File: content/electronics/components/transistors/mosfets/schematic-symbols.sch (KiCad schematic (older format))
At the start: 3 parts, among them Q1 Q_NMOS_DGS, Q2 Q_PMOS_DGS

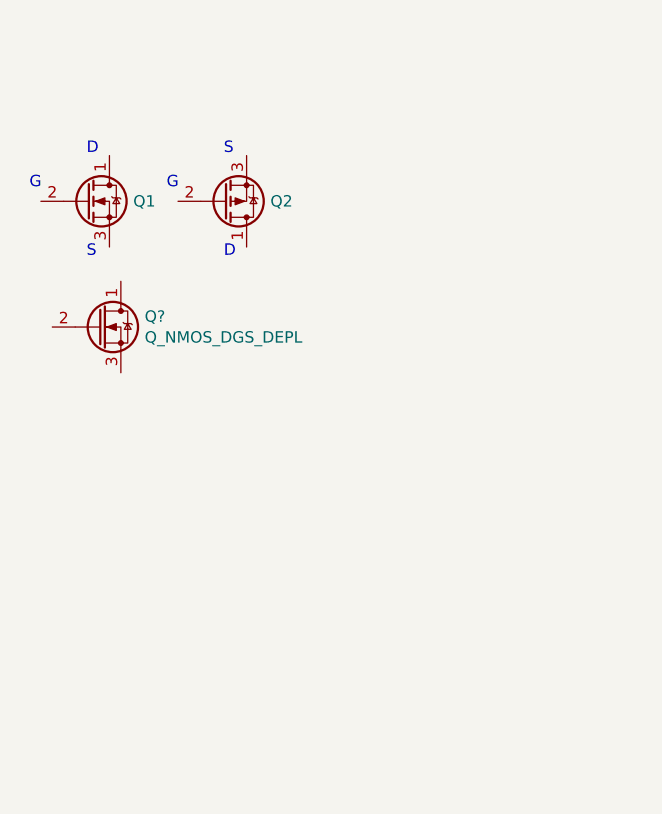
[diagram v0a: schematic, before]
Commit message: Working on MOSFET schematic symbols.
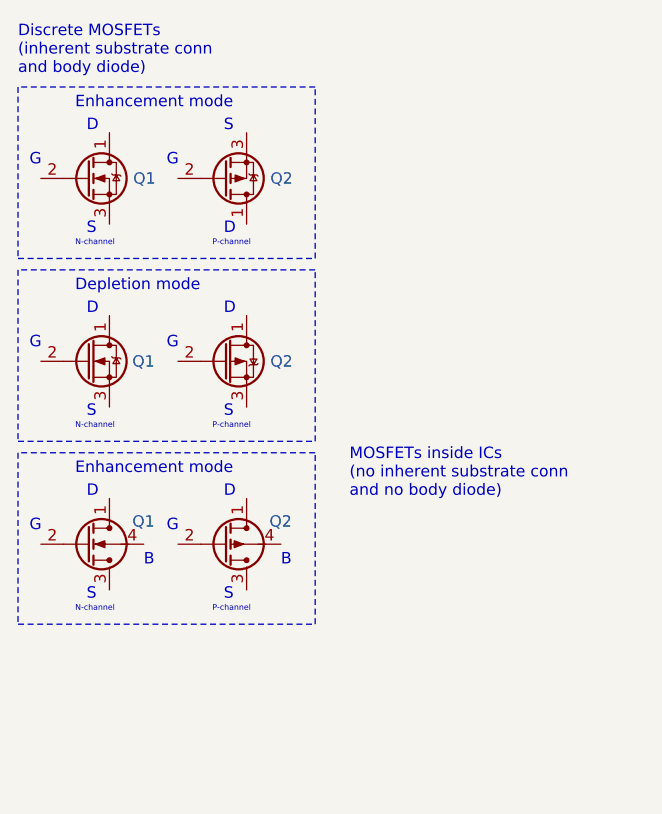
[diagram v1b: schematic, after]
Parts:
- added Q1: Q_NMOS_DGS_4PIN, symbol mbedded-ninja-kicad-symbols:Q_NMOS_DGS_4PIN
- added Q2: Q_PMOS_DGS_DEPL, symbol mbedded-ninja-kicad-symbols:Q_PMOS_DGS_DEPL
- added Q2: Q_PMOS_DGS_4PIN, symbol mbedded-ninja-kicad-symbols:Q_PMOS_DGS_4PIN
- gave numbers to parts that had none: 1
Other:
- note added: "B"
- note added: "Depletion mode"
- note added: "Discrete MOSFETs\n(inherent substrate conn\nand body diode)"
- note added: "Enhancement mode"
- note added: "MOSFETs inside ICs\n(no inherent substrate conn\nand no body diode)"
- note added: "N-channel"
- note added: "P-channel"
- moved on the sheet: Q1, Q2
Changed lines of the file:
@@
 L mbedded-ninja-kicad-symbols:Q_NMOS_DGS Q1
 U 1 1 60235165
-P 4200 3000
-F 0 "Q1" H 4404 3000 50  0000 L CNN
-F 1 "Q_NMOS_DGS" H 4404 2955 50  0001 L CNN
-F 2 "" H 4400 3100 50  0001 C CNN
-F 3 "~" H 4200 3000 50  0001 C CNN
-	1    4200 3000
+P 4200 2900
+F 0 "Q1" H 4404 2900 50  0000 L CNN
+F 1 "Q_NMOS_DGS" H 4404 2855 50  0001 L CNN
+F 2 "" H 4400 3000 50  0001 C CNN
+F 3 "~" H 4200 2900 50  0001 C CNN
+	1    4200 2900
 	1    0    0    -1
 $EndComp
@@
 L mbedded-ninja-kicad-symbols:Q_PMOS_DGS Q2
 U 1 1 60235E64
-P 4800 3000
-F 0 "Q2" H 5004 3000 50  0000 L CNN
-F 1 "Q_PMOS_DGS" H 5005 3045 50  0001 L CNN
-F 2 "" H 5000 3100 50  0001 C CNN
-F 3 "~" H 4800 3000 50  0001 C CNN
-	1    4800 3000
+P 4800 2900
+F 0 "Q2" H 5004 2900 50  0000 L CNN
+F 1 "Q_PMOS_DGS" H 5005 2945 50  0001 L CNN
+F 2 "" H 5000 3000 50  0001 C CNN
+F 3 "~" H 4800 2900 50  0001 C CNN
+	1    4800 2900
 	1    0    0    1
 $EndComp
-Text Notes 3950 2950 0    50   ~ 0
+Text Notes 3950 2850 0    50   ~ 0
 G
-Text Notes 4200 2800 0    50   ~ 0
+Text Notes 4200 2700 0    50   ~ 0
 D
-Text Notes 4200 3250 0    50   ~ 0
+Text Notes 4200 3150 0    50   ~ 0
 S
-Text Notes 4800 2800 0    50   ~ 0
+Text Notes 4800 2700 0    50   ~ 0
 S
-Text Notes 4800 3250 0    50   ~ 0
+Text Notes 4800 3150 0    50   ~ 0
 D
-Text Notes 4550 2950 0    50   ~ 0
+Text Notes 4550 2850 0    50   ~ 0
 G
 $Comp
-L mbedded-ninja-kicad-symbols:Q_NMOS_DGS_DEPL Q?
+L mbedded-ninja-kicad-symbols:Q_NMOS_DGS_DEPL Q1
 U 1 1 6023C375
-P 4250 3550
-F 0 "Q?" H 4454 3596 50  0000 L CNN
-F 1 "Q_NMOS_DGS_DEPL" H 4454 3505 50  0000 L CNN
-F 2 "" H 4450 3650 50  0001 C CNN
-F 3 "~" H 4250 3550 50  0001 C CNN
-	1    4250 3550
+P 4200 3700
+F 0 "Q1" H 4400 3700 50  0000 L CNN
+F 1 "Q_NMOS_DGS_DEPL" H 4404 3655 50  0001 L CNN
+F 2 "" H 4400 3800 50  0001 C CNN
+F 3 "~" H 4200 3700 50  0001 C CNN
+	1    4200 3700
 	1    0    0    -1
 $EndComp
+Text Notes 3900 2450 0    50   ~ 0
+Discrete MOSFETs\n(inherent substrate conn\nand body diode)
+Text Notes 4150 2600 0    50   ~ 0
+Enhancement mode
+Text Notes 4150 3400 0    50   ~ 0
+Depletion mode
+Text Notes 3950 3650 0    50   ~ 0
+G
+Text Notes 4200 3950 0    50   ~ 0
+S
+Text Notes 4200 3500 0    50   ~ 0
+D
+$Comp
+L mbedded-ninja-kicad-symbols:Q_PMOS_DGS_DEPL Q2
+U 1 1 6023A198
+P 4800 3700
+F 0 "Q2" H 5004 3700 50  0000 L CNN
+F 1 "Q_PMOS_DGS_DEPL" H 5005 3655 50  0001 L CNN
+F 2 "" H 5000 3800 50  0001 C CNN
+F 3 "~" H 4800 3700 50  0001 C CNN
+	1    4800 3700
+	1    0    0    -1
+$EndComp
+Wire Notes Line
+	3900 3300 3900 4050
+Wire Notes Line
+	3900 4050 5200 4050
+Wire Notes Line
+	5200 4050 5200 3300
+Wire Notes Line
+	5200 3300 3900 3300
+Text Notes 4150 4000 0    25   ~ 0
+N-channel
+Text Notes 4750 4000 0    25   ~ 0
+P-channel
+Text Notes 4550 3650 0    50   ~ 0
+G
+Text Notes 4800 3500 0    50   ~ 0
+D
+Text Notes 4800 3950 0    50   ~ 0
+S
+Wire Notes Line
+	3900 2500 3900 3250
+Wire Notes Line
+	5200 2500 3900 2500
+Wire Notes Line
+	3900 3250 5200 3250
+Wire Notes Line
+	5200 3250 5200 2500
+Text Notes 4150 3200 0    25   ~ 0
+N-channel
+Text Notes 4750 3200 0    25   ~ 0
+P-channel
+Text Notes 4150 4200 0    50   ~ 0
+Enhancement mode
+Text Notes 3950 4450 0    50   ~ 0
+G
+Text Notes 4200 4750 0    50   ~ 0
+S
+Text Notes 4200 4300 0    50   ~ 0
+D
+Wire Notes Line
+	3900 4100 3900 4850
+Wire Notes Line
+	3900 4850 5200 4850
+Wire Notes Line
+	5200 4850 5200 4100
+Wire Notes Line
+	5200 4100 3900 4100
+Text Notes 4150 4800 0    25   ~ 0
+N-channel
+Text Notes 4750 4800 0    25   ~ 0
+P-channel
+Text Notes 4550 4450 0    50   ~ 0
+G
+Text Notes 4800 4300 0    50   ~ 0
+D
+Text Notes 4800 4750 0    50   ~ 0
+S
+$Comp
+L mbedded-ninja-kicad-symbols:Q_NMOS_DGS_4PIN Q1
+U 1 1 60245762
+P 4200 4500
+F 0 "Q1" H 4400 4600 50  0000 L CNN
+F 1 "Q_NMOS_DGS_4PIN" H 4494 4455 50  0001 L CNN
+F 2 "" H 4400 4600 50  0001 C CNN
+F 3 "~" H 4200 4500 50  0001 C CNN
+	1    4200 4500
+	1    0    0    -1
+$EndComp
+Text Notes 5350 4300 0    50   ~ 0
+MOSFETs inside ICs\n(no inherent substrate conn\nand no body diode)
+$Comp
+L mbedded-ninja-kicad-symbols:Q_PMOS_DGS_4PIN Q2
+U 1 1 60246EE4
+P 4800 4500
+F 0 "Q2" H 5000 4600 50  0000 L CNN
+F 1 "Q_PMOS_DGS_4PIN" H 5094 4455 50  0001 L CNN
+F 2 "" H 5000 4600 50  0001 C CNN
+F 3 "~" H 4800 4500 50  0001 C CNN
+	1    4800 4500
+	1    0    0    -1
+$EndComp
+Text Notes 4450 4600 0    50   ~ 0
+B
+Text Notes 5050 4600 0    50   ~ 0
+B
 $EndSCHEMATC

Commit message: Added alternate style MOSFET symbols to the 'MOSFETs' page.
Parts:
- added Q1: Q_NMOS_NO_BODY, symbol mbedded-ninja-kicad-symbols:Q_NMOS_NO_BODY
- added Q2: Q_PMOS_NO_BODY, symbol mbedded-ninja-kicad-symbols:Q_PMOS_NO_BODY
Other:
- note added: "Alternate Style"
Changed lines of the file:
@@
 Text Notes 5050 4600 0    50   ~ 0
 B
+$Comp
+L mbedded-ninja-kicad-symbols:Q_NMOS_NO_BODY Q1
+U 1 1 6027449C
+P 4200 5300
+F 0 "Q1" H 4350 5300 50  0000 L CNN
+F 1 "Q_NMOS_NO_BODY" H 4388 5255 50  0001 L CNN
+F 2 "" H 4400 5400 50  0001 C CNN
+F 3 "~" H 4200 5300 50  0001 C CNN
+	1    4200 5300
+	1    0    0    -1
+$EndComp
+Text Notes 4250 5000 0    50   ~ 0
+Alternate Style
+Text Notes 3950 5250 0    50   ~ 0
+G
+Text Notes 4200 5550 0    50   ~ 0
+S
+Text Notes 4200 5100 0    50   ~ 0
+D
+Text Notes 4150 5600 0    25   ~ 0
+N-channel
+Text Notes 4750 5600 0    25   ~ 0
+P-channel
+Text Notes 4550 5250 0    50   ~ 0
+G
+Text Notes 4800 5100 0    50   ~ 0
+D
+Text Notes 4800 5550 0    50   ~ 0
+S
+$Comp
+L mbedded-ninja-kicad-symbols:Q_PMOS_NO_BODY Q2
+U 1 1 60279B91
+P 4800 5300
+F 0 "Q2" H 4950 5300 50  0000 L CNN
+F 1 "Q_PMOS_NO_BODY" H 4988 5345 50  0001 L CNN
+F 2 "" H 5000 5400 50  0001 C CNN
+F 3 "~" H 4800 5300 50  0001 C CNN
+	1    4800 5300
+	1    0    0    1
+$EndComp
 $EndSCHEMATC
